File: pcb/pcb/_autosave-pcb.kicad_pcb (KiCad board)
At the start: 2 copper layers, 41 x 41 mm, 16 parts, among them U1 rp2040-zero

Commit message: added full version
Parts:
- added G***: LOGO, LOGO, F.Cu at (149.7, 42.9)
- added R5: 220 Ω, Resistor_SMD:R_1206_3216Metric_Pad1.30x1.75mm_HandSolder, F.Cu at (159.0, 65.5)
- moved G*** 1.21 mm to (149.7, 51.2)
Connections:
- U1 pad 7: Net-(BZ1-+) -> Net-(U1-6)
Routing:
- net Net-(U1-6): track 0.00 -> 22.2 mm, vias 0 -> 3
- net Net-(BZ1-+): track 21.3 -> 12.5 mm, vias 3 -> 0
- added copper zone on F.Cu, net (none)
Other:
- board text added: "->"
- board text added: "BEEP"
- board text added: "Simon Game Clone"
- board text added: "TWIM"
- board text removed: "COLOR_REPETER"

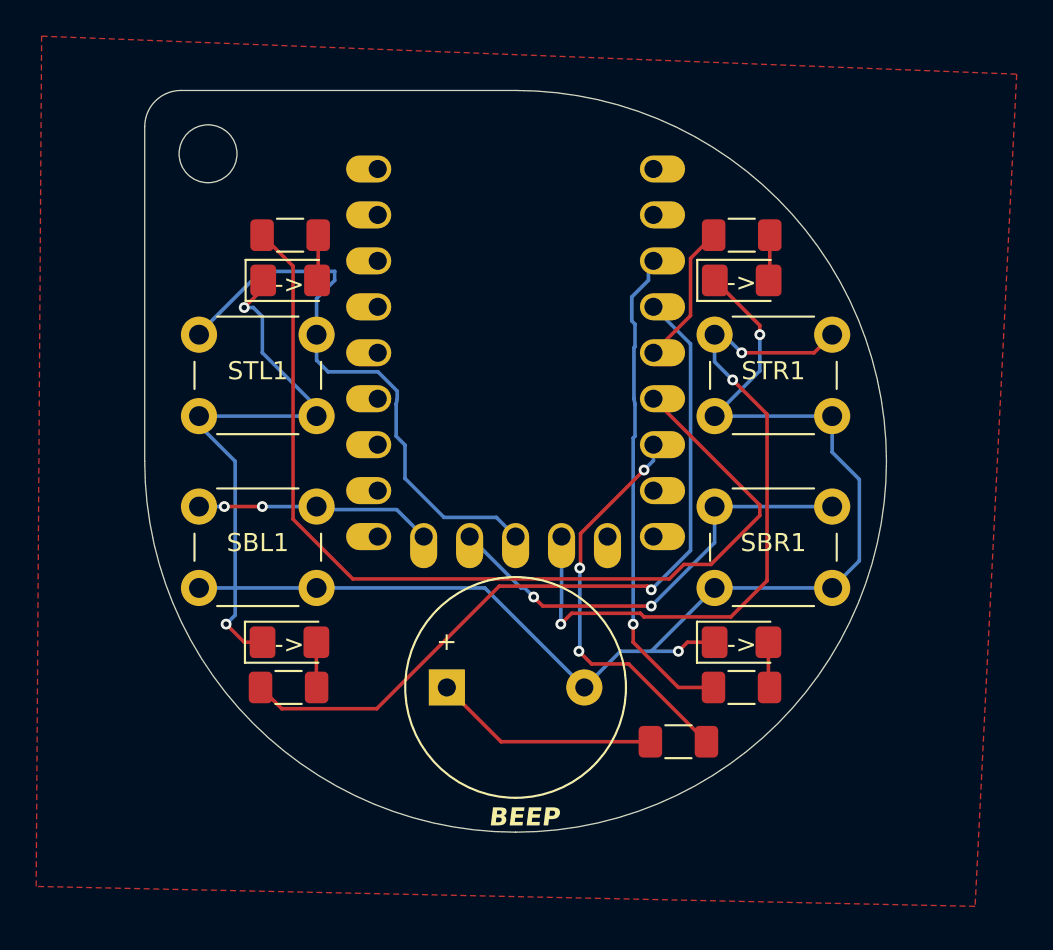
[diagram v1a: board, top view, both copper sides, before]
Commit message: updated gerbers and transition to pi pico
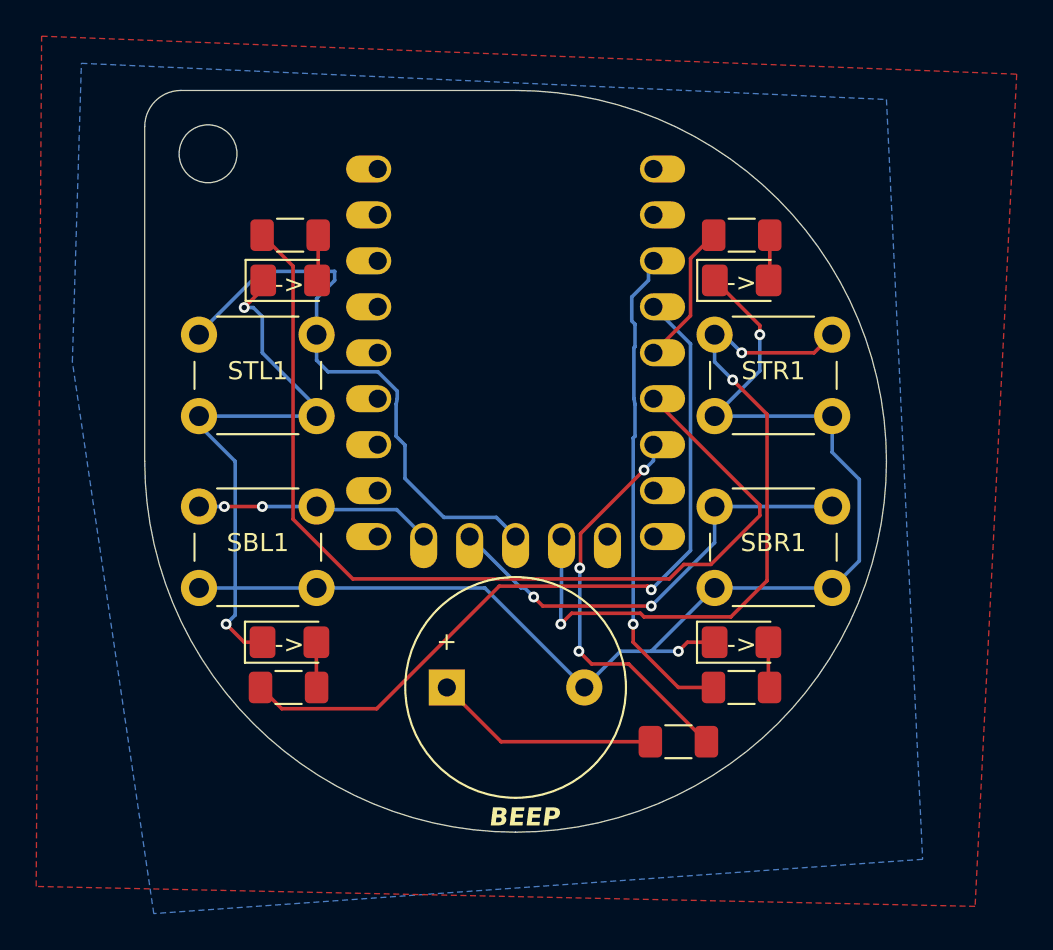
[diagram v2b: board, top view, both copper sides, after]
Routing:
- added copper zone on B.Cu, net (none)
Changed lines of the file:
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@@
 		)
 		(property "Value" "220 Ω"
-			(at 0 1.82 360)
+			(at 0 1.82 0)
 			(layer "F.Fab")
 			(effects
@@
 		(min_thickness 0.25)
 		(filled_areas_thickness no)
-		(fill
+		(fill yes
 			(thermal_gap 0.5)
 			(thermal_bridge_width 0.5)
@@
 			)
 		)
+	)
+	(zone
+		(net 0)
+		(net_name "")
+		(layer "B.Cu")
+		(hatch edge 0.5)
+		(priority 1)
+		(connect_pads
+			(clearance 0.5)
+		)
+		(min_thickness 0.25)
+		(filled_areas_thickness no)
+		(fill yes
+			(thermal_gap 0.5)
+			(thermal_bridge_width 0.5)
+			(island_removal_mode 1)
+			(island_area_min 10)
+		)
+		(polygon
+			(pts
+				(xy 126 28) (xy 170.5 30) (xy 172.5 72) (xy 130 75) (xy 125.5 44.5)
+			)
+		)
